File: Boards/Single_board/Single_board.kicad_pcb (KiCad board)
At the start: 2 copper layers, 169.9 x 190.9 mm, 116 parts, among them J1 POWER, J2 ICSP, J3 USB_C_Receptacle_USB2.0_16P, J4 USB_C_Receptacle_USB2.0_16P, J5 USB_C_Receptacle_USB2.0_16P, SW1 +, SW10 5, SW11 2, SW12 9, SW13 PRO, SW14 6, SW15 3, SW16 CLR, SW17 ENTR, SW18 RSET, SW19 KEYREL, SW2 VERB, SW3 NOUN, SW4 0, SW5 7, SW6 -, SW7 4, SW8 1, SW9 8, U2 ATmega328P-A, U3 CH340C

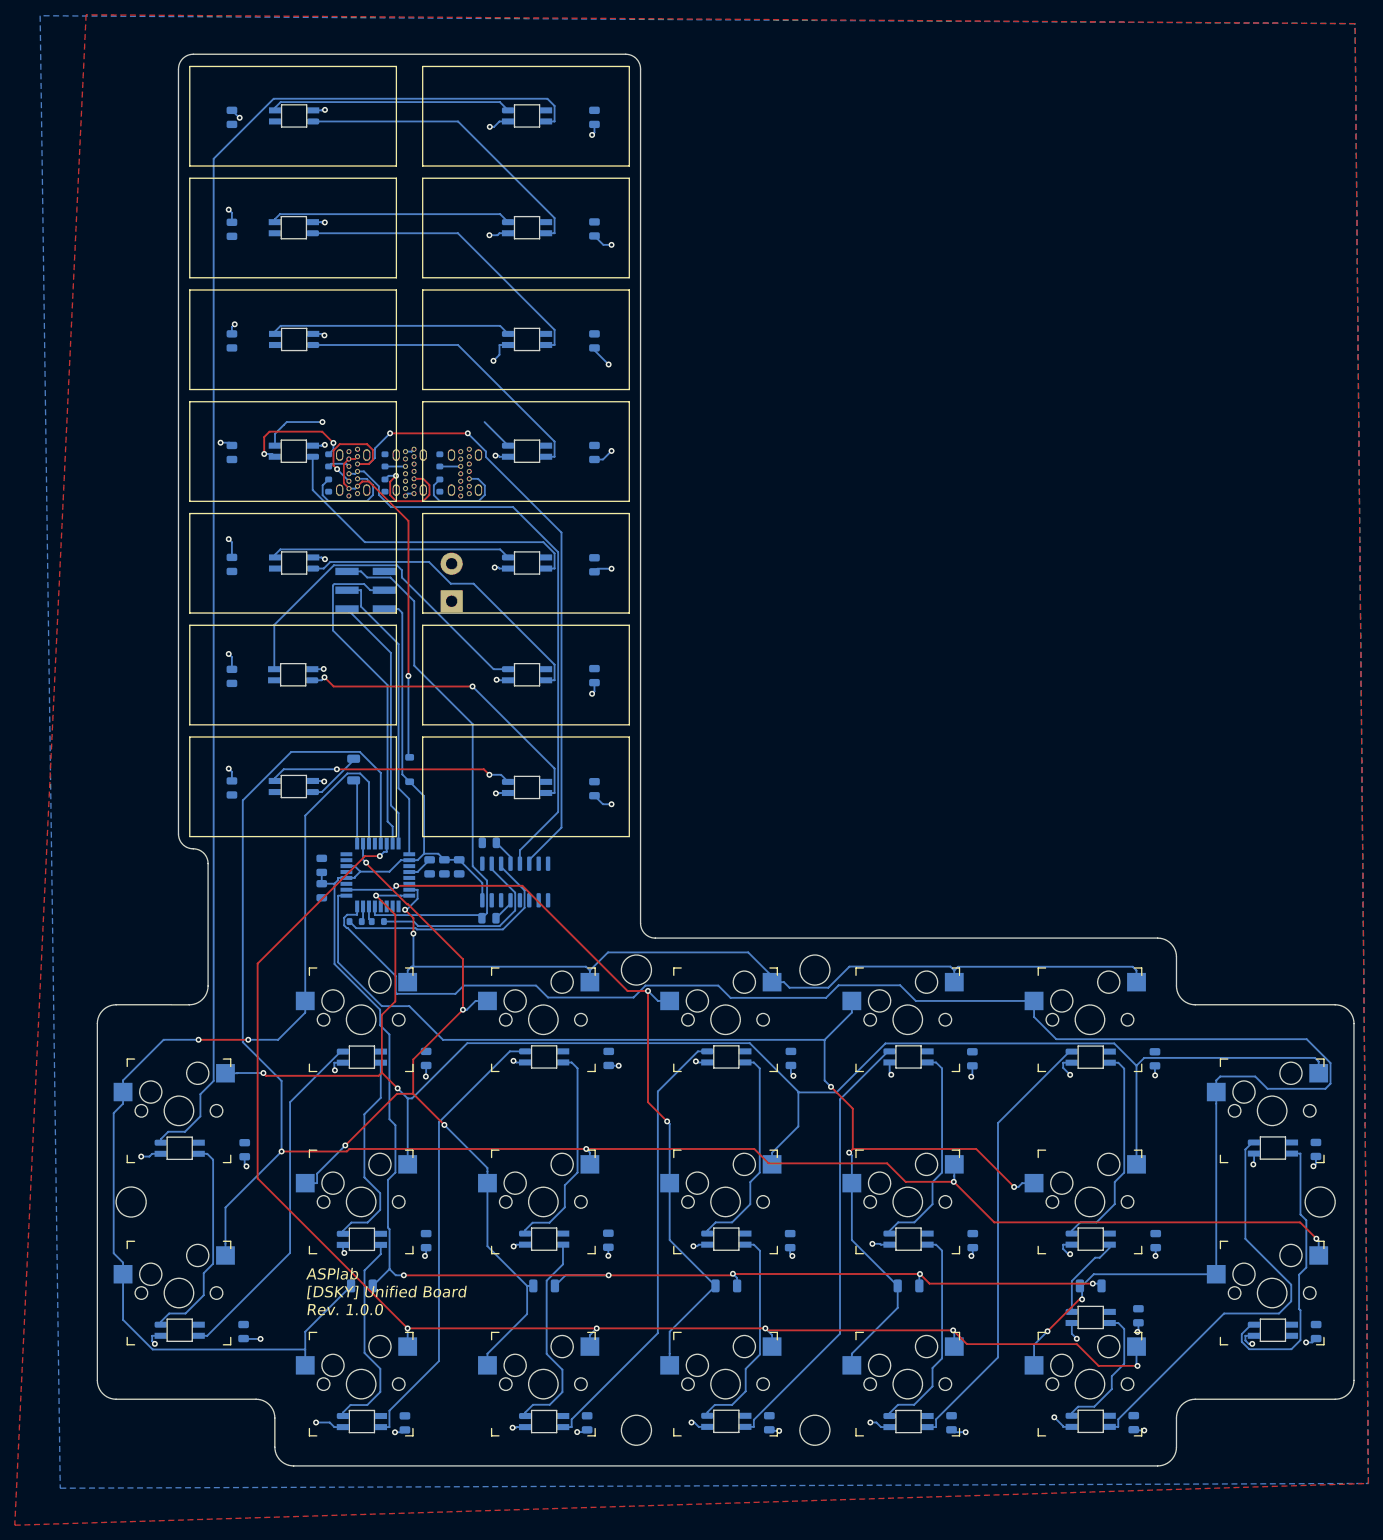
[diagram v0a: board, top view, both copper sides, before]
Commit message: Small routing improvements and prepare for JLC order
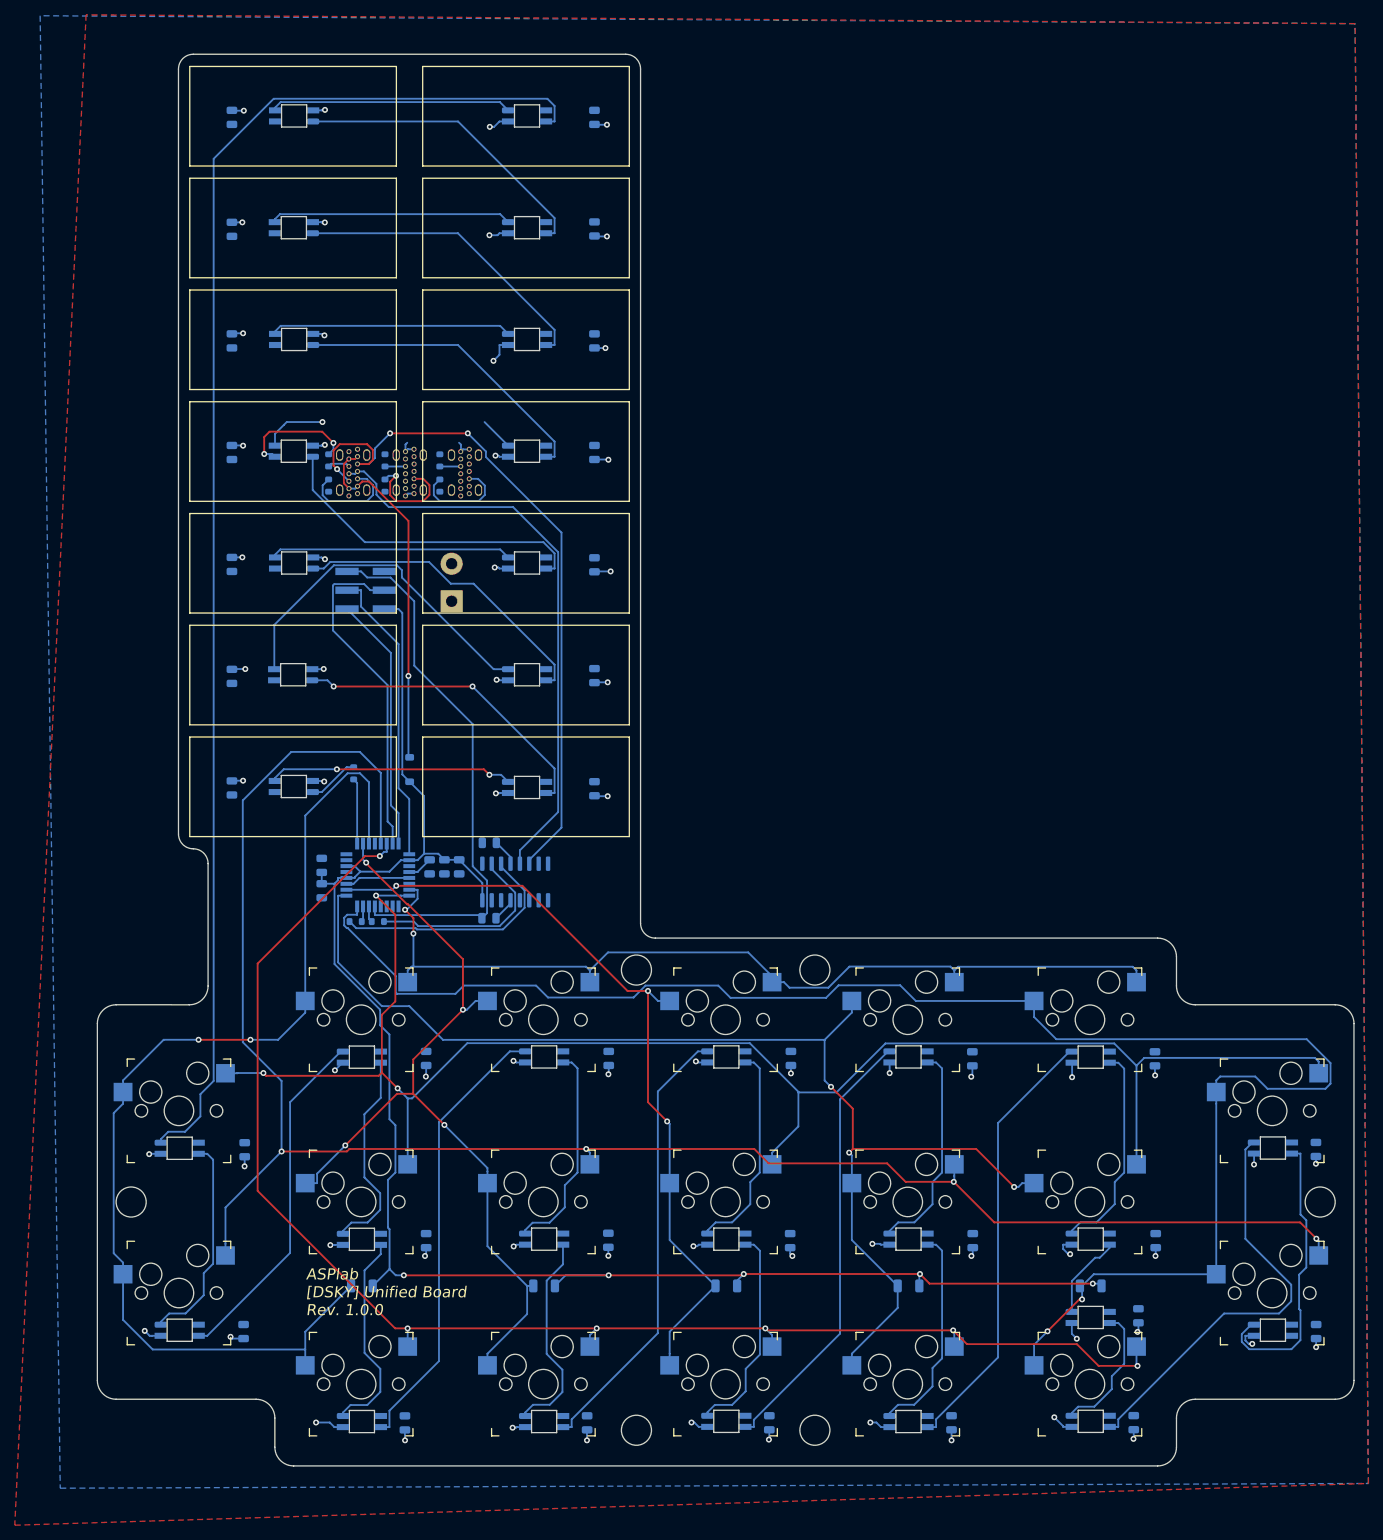
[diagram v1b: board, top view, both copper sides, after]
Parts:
- C1, C5: footprint Capacitor_SMD:C_0805_2012Metric -> Project Libraries:0805 4.7uF
- C10, C11, C12, C13, C14, C15, C16, C17, C18, C19, C2, C20, C21, C22, C23, C24, C25, C26, C27, C28, C29, C3, C30, C31, C32, C33, C34, C35, C36, C37, C38, C39, C4, C40, C41, C6, C7, C8, C9: footprint Capacitor_SMD:C_0805_2012Metric -> Project Libraries:0805 100nF
- R1: value 500 -> 470; footprint Resistor_SMD:R_1206_3216Metric -> Resistor_SMD:R_0603_1608Metric
- SW1: value + -> 2V~12V SMD Mechanical Keyboard Shaft ROHS
- SW10: value 5 -> 2V~12V SMD Mechanical Keyboard Shaft ROHS
- SW11: value 2 -> 2V~12V SMD Mechanical Keyboard Shaft ROHS
- SW12: value 9 -> 2V~12V SMD Mechanical Keyboard Shaft ROHS
- SW13: value PRO -> 2V~12V SMD Mechanical Keyboard Shaft ROHS
- SW14: value 6 -> 2V~12V SMD Mechanical Keyboard Shaft ROHS
- SW15: value 3 -> 2V~12V SMD Mechanical Keyboard Shaft ROHS
- SW16: value CLR -> 2V~12V SMD Mechanical Keyboard Shaft ROHS
- SW17: value ENTR -> 2V~12V SMD Mechanical Keyboard Shaft ROHS
- SW18: value RSET -> 2V~12V SMD Mechanical Keyboard Shaft ROHS
- SW19: value KEYREL -> 2V~12V SMD Mechanical Keyboard Shaft ROHS
- SW2: value VERB -> 2V~12V SMD Mechanical Keyboard Shaft ROHS
- SW3: value NOUN -> 2V~12V SMD Mechanical Keyboard Shaft ROHS
- SW4: value 0 -> 2V~12V SMD Mechanical Keyboard Shaft ROHS
- SW5: value 7 -> 2V~12V SMD Mechanical Keyboard Shaft ROHS
- SW6: value - -> 2V~12V SMD Mechanical Keyboard Shaft ROHS
- SW7: value 4 -> 2V~12V SMD Mechanical Keyboard Shaft ROHS
- SW8: value 1 -> 2V~12V SMD Mechanical Keyboard Shaft ROHS
- SW9: value 8 -> 2V~12V SMD Mechanical Keyboard Shaft ROHS
- moved R1 0.51 mm to (157.4, 133.0)
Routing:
- net GND: track 18.5 -> 31.2 mm
- net 5V10A: track 133.6 -> 120.9 mm
- net Y3: track 196.5 -> 197.5 mm
- net Net-(D2-DOUT): track 42.6 -> 41.9 mm
- net Net-(D1-DIN): track 7.52 -> 6.93 mm

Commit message: JLC adjustments
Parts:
- J3, J4, J5: value USB_C_Receptacle_USB2.0_16P -> 918-468K2029E50001
- R10, R2, R3, R44, R45, R9: value 5.1k -> 0603WAF5101T5E
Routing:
- net 5V10A: track 120.9 -> 119.2 mm
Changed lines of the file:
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@@
 		(tags "capacitor")
 		(property "Reference" "C1"
-			(at 0 1.68 90)
+			(at 2.75 0.02 90)
 			(layer "B.SilkS")
 			(effects
@@
 		)
 		(property "Value" "4.7uF"
-			(at 0 -3.5 90)
+			(at -3.85 0.02 90)
 			(layer "B.Fab")
 			(effects
@@
 			)
 		)
-		(property "Value" "5.1k"
+		(property "Value" "0603WAF5101T5E"
 			(at -6.0452 0 90)
 			(layer "B.Fab")
+			(hide yes)
 			(effects
 				(font
@@
 			)
 		)
-		(property "Value" "5.1k"
+		(property "Value" "0603WAF5101T5E"
 			(at -5.1816 0 90)
 			(layer "B.Fab")
+			(hide yes)
 			(effects
 				(font
@@
 			)
 		)
-		(property "Value" "USB_C_Receptacle_USB2.0_16P"
+		(property "Value" "918-468K2029E50001"
 			(at 0 -7.16 0)
 			(layer "B.Fab")
@@
 		)
 		(property "Value" "100nF"
-			(at 0 -3.5 0)
+			(at -0.005 2 0)
 			(layer "B.Fab")
 			(effects
@@
 		)
 		(property "Value" "100nF"
-			(at 0 -3.5 -90)
+			(at 0.05 -3.832 180)
 			(layer "B.Fab")
 			(effects
@@
 		)
 		(fp_text user "${REFERENCE}"
-			(at 0 -2 -90)
+			(at 0.05 -0.132 -90)
 			(layer "B.Fab")
 			(effects
@@
 		)
 		(property "Value" "4.7uF"
-			(at 0 -3.5 90)
+			(at 0 3.4354 180)
 			(layer "B.Fab")
 			(effects
@@
 		(tags "SOIC SO")
 		(property "Reference" "U3"
-			(at -4.8 -4.2 0)
+			(at 0 -6.005 90)
 			(layer "B.SilkS")
 			(effects
@@
 		)
 		(property "Value" "CH340C"
-			(at -1.4 -6.2 90)
+			(at 0.2 -0.005 180)
 			(layer "B.Fab")
 			(effects
@@
 			(layer "B.Fab")
 		)
-		(fp_text user "${REFERENCE}"
-			(at 0 0 90)
-			(layer "B.Fab")
-			(effects
-				(font
-					(size 0.98 0.98)
-					(thickness 0.15)
-				)
-				(justify mirror)
-			)
-		)
 		(pad "1" smd roundrect
 			(at -2.475 4.445 270)
@@
 			)
 		)
-		(property "Value" "5.1k"
+		(property "Value" "0603WAF5101T5E"
 			(at 5.1816 -0.0508 90)
 			(layer "B.Fab")
+			(hide yes)
 			(effects
 				(font
@@
 		(tags "capacitor")
 		(property "Reference" "C7"
-			(at 0 1.68 90)
+			(at 2.75 0.02 90)
 			(layer "B.SilkS")
 			(effects
@@
 		)
 		(property "Value" "100nF"
-			(at 0 -3.5 90)
+			(at -4.05 0.02 90)
 			(layer "B.Fab")
 			(effects
@@
 		(tags "capacitor")
 		(property "Reference" "C2"
-			(at 0 1.68 90)
+			(at 2.75 0.02 90)
 			(layer "B.SilkS")
 			(effects
@@
 		)
 		(property "Value" "100nF"
-			(at 0 -3.5 90)
+			(at -4.25 0.02 90)
 			(layer "B.Fab")
 			(effects
@@
 			)
 		)
-		(property "Value" "USB_C_Receptacle_USB2.0_16P"
+		(property "Value" "918-468K2029E50001"
 			(at 0 -7.16 0)
 			(layer "B.Fab")
@@
 		)
 		(property "Value" "100nF"
-			(at 0 -3.5 0)
+			(at 0 -1.5 0)
 			(layer "B.Fab")
 			(effects
@@
 		)
 		(fp_text user "${REFERENCE}"
-			(at 0 -2 0)
+			(at 0 -0.1 0)
 			(layer "B.Fab")
 			(effects
@@
 			)
 		)
-		(property "Value" "5.1k"
+		(property "Value" "0603WAF5101T5E"
 			(at 6.0452 -0.0508 90)
 			(layer "B.Fab")
+			(hide yes)
 			(effects
 				(font
@@
 		(tags "resistor")
 		(property "Reference" "R1"
-			(at -2.4 0.0516 -90)
+			(at -2.4 0.0516 0)
 			(layer "B.SilkS")
 			(effects
@@
 			)
 		)
-		(property "Value" "USB_C_Receptacle_USB2.0_16P"
+		(property "Value" "918-468K2029E50001"
 			(at 0 -7.16 0)
 			(layer "B.Fab")
@@
 			)
 		)
-		(property "Value" "5.1k"
+		(property "Value" "0603WAF5101T5E"
 			(at -6.096 0.0508 90)
 			(layer "B.Fab")
+			(hide yes)
 			(effects
 				(font
@@
 			)
 		)
-		(property "Value" "5.1k"
+		(property "Value" "0603WAF5101T5E"
 			(at -6.2992 0 90)
 			(layer "B.Fab")
+			(hide yes)
 			(effects
 				(font
@@
 		(tags "QFP 0.8")
 		(property "Reference" "U2"
-			(at -5 -5 0)
+			(at 0.08 -6.15 0)
 			(layer "B.SilkS")
 			(effects
@@
 			(at 0 -6.05 0)
 			(layer "B.Fab")
+			(hide yes)
 			(effects
 				(font
@@
 	)
 	(via
+		(at 176.33 74.969)
+		(size 0.8)
+		(drill 0.4)
+		(layers "F.Cu" "B.Cu")
+		(net 77)
+	)
+	(via
 		(at 227.5259 196.5945)
 		(size 0.8)
@@
 	)
 	(via
-		(at 176.2857 77.1942)
-		(size 0.8)
-		(drill 0.4)
-		(layers "F.Cu" "B.Cu")
-		(net 77)
-	)
-	(via
 		(at 240.8916 174.0013)
 		(size 0.8)
@@
 	)
 	(segment
-		(start 177.0999 76.38)
-		(end 177.0999 75.054)
-		(width 0.25)
-		(layer "B.Cu")
-		(net 77)
-	)
-	(segment
 		(start 189.988 45.269)
 		(end 189.9412 45.2222)
@@
 	)
 	(segment
-		(start 178.275 75.054)
-		(end 177.0999 75.054)
-		(width 0.25)
-		(layer "B.Cu")
-		(net 77)
-	)
-	(segment
 		(start 154.1495 220.7573)
 		(end 154.7709 221.3787)
@@
 	)
 	(segment
-		(start 176.2857 77.1942)
-		(end 177.0999 76.38)
-		(width 0.25)
-		(layer "B.Cu")
-		(net 77)
-	)
-	(segment
 		(start 129.73 184.469)
 		(end 129.7773 184.4217)
@@
 	)
 	(segment
+		(start 178.275 75.054)
+		(end 176.415 75.054)
+		(width 0.25)
+		(layer "B.Cu")
+		(net 77)
+	)
+	(segment
 		(start 277.9609 209.6678)
 		(end 277.9609 209.03)
@@
 		(width 0.25)
 		(layer "B.Cu")
+		(net 77)
+	)
+	(segment
+		(start 176.415 75.054)
+		(end 176.33 74.969)
+		(width 0.25)
+		(layer "B.Cu")
